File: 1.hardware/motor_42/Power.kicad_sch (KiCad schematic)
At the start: 24 parts, among them U1 TPS54202DDC

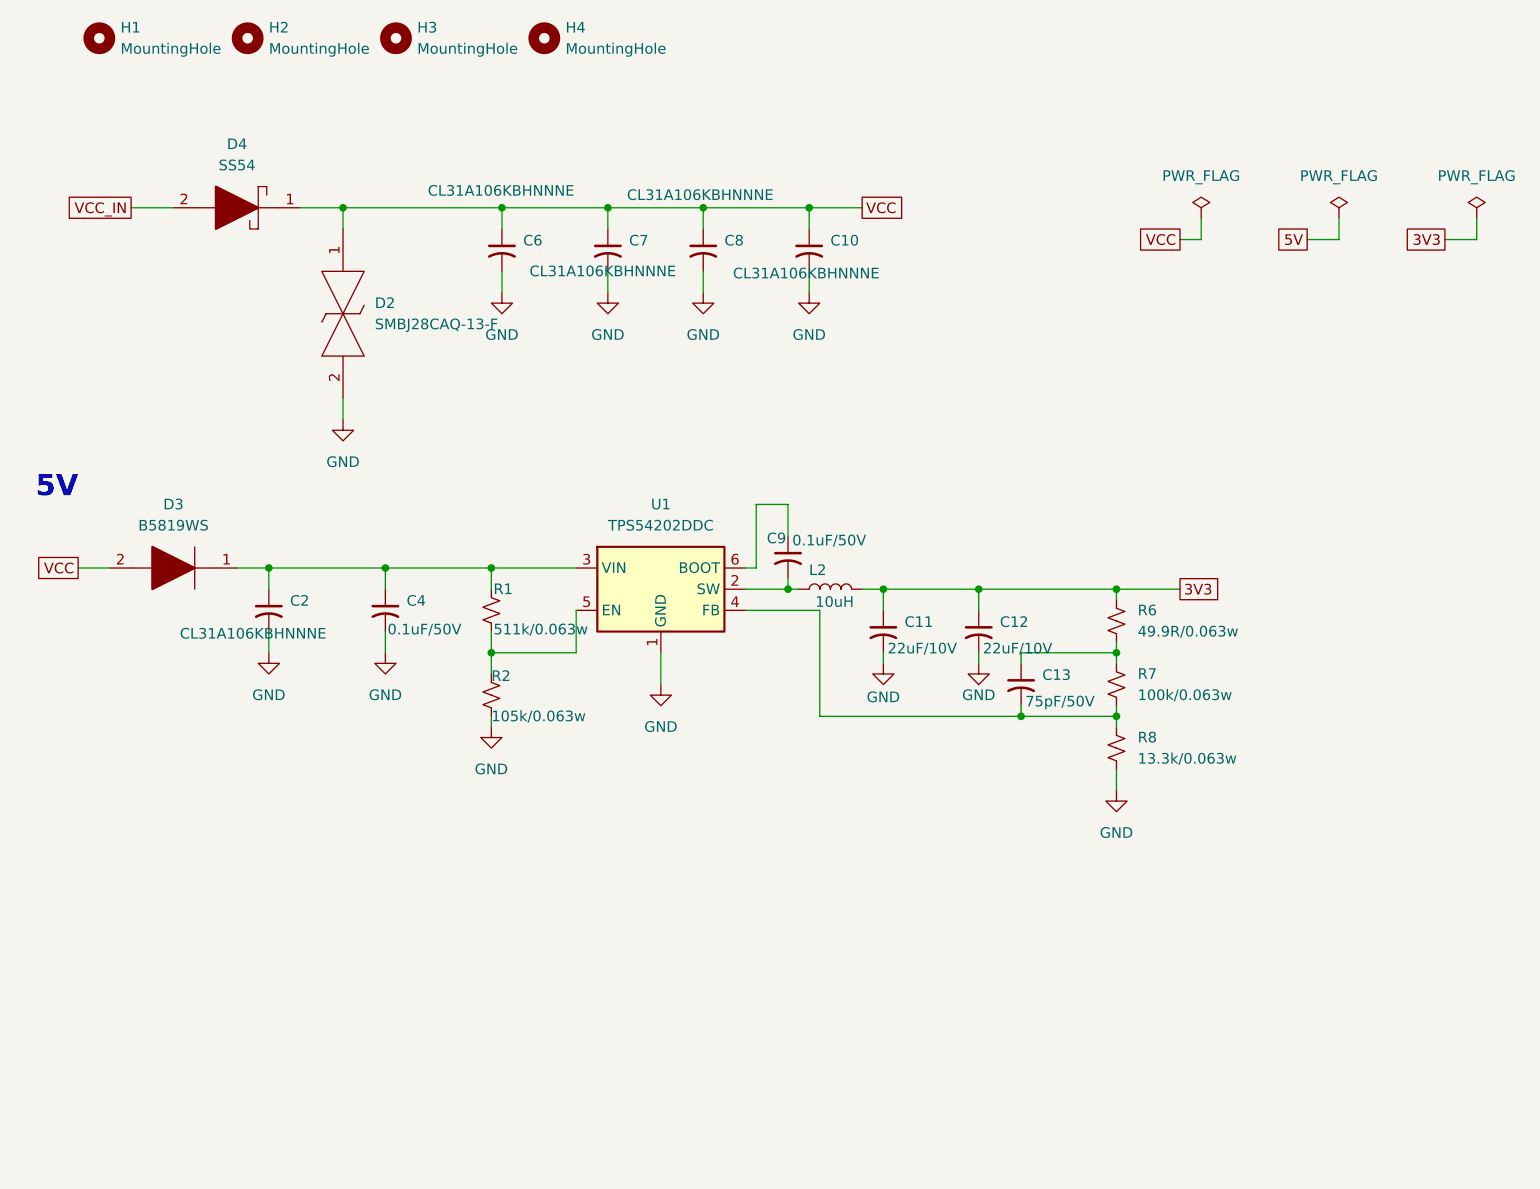
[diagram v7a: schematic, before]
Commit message: 번호 초기화 및 led 변경
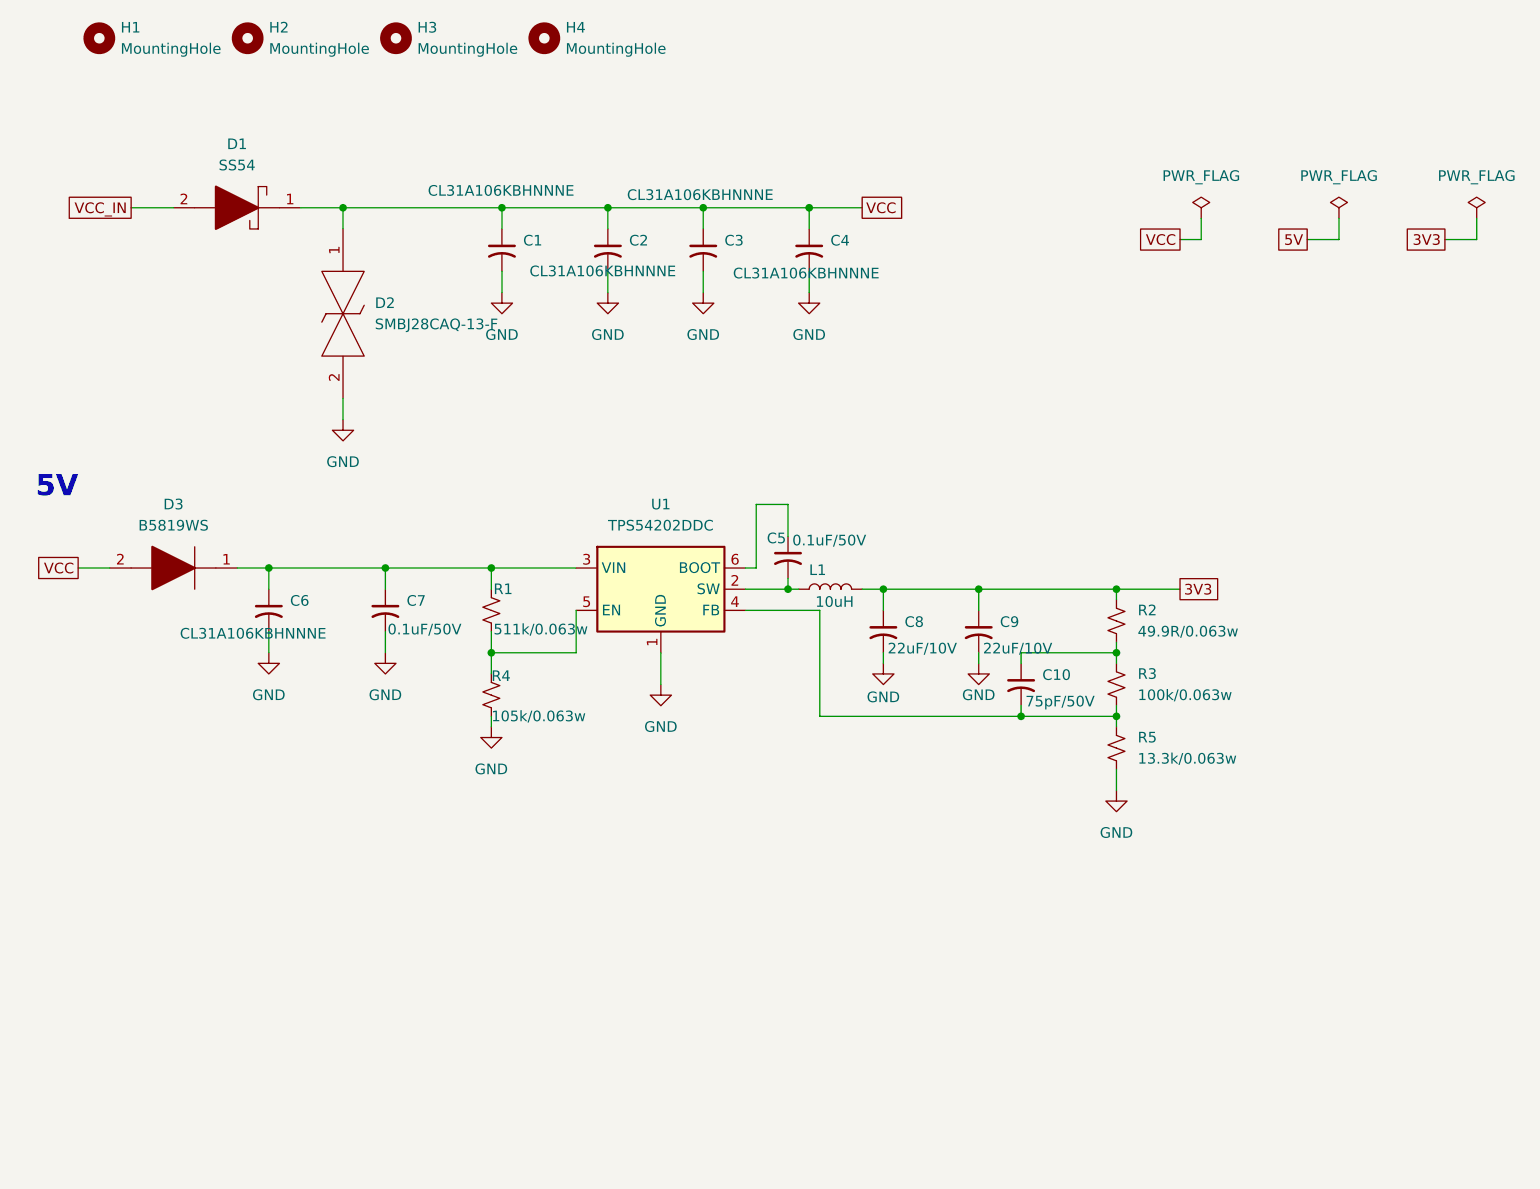
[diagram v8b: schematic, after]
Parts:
- renumbered C6 to C1, C13 to C10, C7 to C2, C8 to C3, C10 to C4, C9 to C5, C2 to C6, C4 to C7, C11 to C8, C12 to C9, D4 to D1, L2 to L1, R6 to R2, R7 to R3, R2 to R4, R8 to R5
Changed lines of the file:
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@@
 		(on_board yes)
 		(dnp no)
-		(property "Reference" "C2"
+		(property "Reference" "C6"
 			(at 57.15 92.8369 0)
 			(effects
@@
 			(project ""
 				(path "/3c5de6a8-6840-43a5-a2fb-24dbb7f0450d/79279b58-6f84-47a5-8a20-31a3cd7584cf"
-					(reference "C2")
+					(reference "C6")
 					(unit 1)
 				)
@@
 		(dnp no)
 		(fields_autoplaced yes)
-		(property "Reference" "#PWR02"
+		(property "Reference" "#PWR06"
 			(at 54.61 105.41 0)
 			(effects
@@
 			(project "motor_42"
 				(path "/3c5de6a8-6840-43a5-a2fb-24dbb7f0450d/79279b58-6f84-47a5-8a20-31a3cd7584cf"
-					(reference "#PWR02")
+					(reference "#PWR06")
 					(unit 1)
 				)
@@
 		(dnp no)
 		(fields_autoplaced yes)
-		(property "Reference" "D4"
+		(property "Reference" "D1"
 			(at 50.8 38.1 0)
 			(effects
@@
 			(project ""
 				(path "/3c5de6a8-6840-43a5-a2fb-24dbb7f0450d/79279b58-6f84-47a5-8a20-31a3cd7584cf"
-					(reference "D4")
+					(reference "D1")
 					(unit 1)
 				)
@@
 		(on_board yes)
 		(dnp no)
-		(property "Reference" "C6"
+		(property "Reference" "C1"
 			(at 85.09 49.6569 0)
 			(effects
@@
 			(project "motor_42"
 				(path "/3c5de6a8-6840-43a5-a2fb-24dbb7f0450d/79279b58-6f84-47a5-8a20-31a3cd7584cf"
-					(reference "C6")
+					(reference "C1")
 					(unit 1)
 				)
@@
 		(on_board yes)
 		(dnp no)
-		(property "Reference" "L2"
+		(property "Reference" "L1"
 			(at 120.396 89.154 90)
 			(effects
@@
 			(project ""
 				(path "/3c5de6a8-6840-43a5-a2fb-24dbb7f0450d/79279b58-6f84-47a5-8a20-31a3cd7584cf"
-					(reference "L2")
+					(reference "L1")
 					(unit 1)
 				)
@@
 		(dnp no)
 		(fields_autoplaced yes)
-		(property "Reference" "#PWR016"
+		(property "Reference" "#PWR012"
 			(at 156.21 121.92 0)
 			(effects
@@
 			(project "motor_42"
 				(path "/3c5de6a8-6840-43a5-a2fb-24dbb7f0450d/79279b58-6f84-47a5-8a20-31a3cd7584cf"
-					(reference "#PWR016")
+					(reference "#PWR012")
 					(unit 1)
 				)
@@
 		(on_board yes)
 		(dnp no)
-		(property "Reference" "C10"
+		(property "Reference" "C4"
 			(at 121.92 49.6569 0)
 			(effects
@@
 			(project "motor_42"
 				(path "/3c5de6a8-6840-43a5-a2fb-24dbb7f0450d/79279b58-6f84-47a5-8a20-31a3cd7584cf"
-					(reference "C10")
+					(reference "C4")
 					(unit 1)
 				)
@@
 		(dnp no)
 		(fields_autoplaced yes)
-		(property "Reference" "#PWR011"
+		(property "Reference" "#PWR03"
 			(at 106.68 62.23 0)
 			(effects
@@
 			(project "motor_42"
 				(path "/3c5de6a8-6840-43a5-a2fb-24dbb7f0450d/79279b58-6f84-47a5-8a20-31a3cd7584cf"
-					(reference "#PWR011")
+					(reference "#PWR03")
 					(unit 1)
 				)
@@
 		(on_board yes)
 		(dnp no)
-		(property "Reference" "R2"
+		(property "Reference" "R4"
 			(at 81.28 101.854 0)
 			(effects
@@
 			(project "motor_42"
 				(path "/3c5de6a8-6840-43a5-a2fb-24dbb7f0450d/79279b58-6f84-47a5-8a20-31a3cd7584cf"
-					(reference "R2")
+					(reference "R4")
 					(unit 1)
 				)
@@
 		(on_board yes)
 		(dnp no)
-		(property "Reference" "C13"
+		(property "Reference" "C10"
 			(at 147.32 101.7269 0)
 			(effects
@@
 			(project "motor_42"
 				(path "/3c5de6a8-6840-43a5-a2fb-24dbb7f0450d/79279b58-6f84-47a5-8a20-31a3cd7584cf"
-					(reference "C13")
+					(reference "C10")
 					(unit 1)
 				)
@@
 		(dnp no)
 		(fields_autoplaced yes)
-		(property "Reference" "R6"
+		(property "Reference" "R2"
 			(at 158.75 93.9799 0)
 			(effects
@@
 			(project "motor_42"
 				(path "/3c5de6a8-6840-43a5-a2fb-24dbb7f0450d/79279b58-6f84-47a5-8a20-31a3cd7584cf"
-					(reference "R6")
+					(reference "R2")
 					(unit 1)
 				)
@@
 		(on_board yes)
 		(dnp no)
-		(property "Reference" "C4"
+		(property "Reference" "C7"
 			(at 71.12 92.8369 0)
 			(effects
@@
 			(project "motor_42"
 				(path "/3c5de6a8-6840-43a5-a2fb-24dbb7f0450d/79279b58-6f84-47a5-8a20-31a3cd7584cf"
-					(reference "C4")
+					(reference "C7")
 					(unit 1)
 				)
@@
 		(dnp no)
 		(fields_autoplaced yes)
-		(property "Reference" "#PWR013"
+		(property "Reference" "#PWR04"
 			(at 119.38 62.23 0)
 			(effects
@@
 			(project "motor_42"
 				(path "/3c5de6a8-6840-43a5-a2fb-24dbb7f0450d/79279b58-6f84-47a5-8a20-31a3cd7584cf"
-					(reference "#PWR013")
+					(reference "#PWR04")
 					(unit 1)
 				)
@@
 		(dnp no)
 		(fields_autoplaced yes)
-		(property "Reference" "#PWR04"
+		(property "Reference" "#PWR05"
 			(at 63.5 77.47 0)
 			(effects
@@
 			(project "motor_42"
 				(path "/3c5de6a8-6840-43a5-a2fb-24dbb7f0450d/79279b58-6f84-47a5-8a20-31a3cd7584cf"
-					(reference "#PWR04")
+					(reference "#PWR05")
 					(unit 1)
 				)
@@
 		(dnp no)
 		(fields_autoplaced yes)
-		(property "Reference" "R8"
+		(property "Reference" "R5"
 			(at 158.75 109.2199 0)
 			(effects
@@
 			(project "motor_42"
 				(path "/3c5de6a8-6840-43a5-a2fb-24dbb7f0450d/79279b58-6f84-47a5-8a20-31a3cd7584cf"
-					(reference "R8")
+					(reference "R5")
 					(unit 1)
 				)
@@
 		(on_board yes)
 		(dnp no)
-		(property "Reference" "C7"
+		(property "Reference" "C2"
 			(at 97.79 49.6569 0)
 			(effects
@@
 			(project "motor_42"
 				(path "/3c5de6a8-6840-43a5-a2fb-24dbb7f0450d/79279b58-6f84-47a5-8a20-31a3cd7584cf"
-					(reference "C7")
+					(reference "C2")
 					(unit 1)
 				)
@@
 		(on_board yes)
 		(dnp no)
-		(property "Reference" "#PWR015"
+		(property "Reference" "#PWR09"
 			(at 139.7 106.68 0)
 			(effects
@@
 			(project "motor_42"
 				(path "/3c5de6a8-6840-43a5-a2fb-24dbb7f0450d/79279b58-6f84-47a5-8a20-31a3cd7584cf"
-					(reference "#PWR015")
+					(reference "#PWR09")
 					(unit 1)
 				)
@@
 		(dnp no)
 		(fields_autoplaced yes)
-		(property "Reference" "#PWR09"
+		(property "Reference" "#PWR02"
 			(at 95.25 62.23 0)
 			(effects
@@
 			(project "motor_42"
 				(path "/3c5de6a8-6840-43a5-a2fb-24dbb7f0450d/79279b58-6f84-47a5-8a20-31a3cd7584cf"
-					(reference "#PWR09")
+					(reference "#PWR02")
 					(unit 1)
 				)
@@
 		(dnp no)
 		(fields_autoplaced yes)
-		(property "Reference" "R7"
+		(property "Reference" "R3"
 			(at 158.75 101.5999 0)
 			(effects
@@
 			(project ""
 				(path "/3c5de6a8-6840-43a5-a2fb-24dbb7f0450d/79279b58-6f84-47a5-8a20-31a3cd7584cf"
-					(reference "R7")
+					(reference "R3")
 					(unit 1)
 				)
@@
 		(dnp no)
 		(fields_autoplaced yes)
-		(property "Reference" "#PWR08"
+		(property "Reference" "#PWR01"
 			(at 82.55 62.23 0)
 			(effects
@@
 			(project "motor_42"
 				(path "/3c5de6a8-6840-43a5-a2fb-24dbb7f0450d/79279b58-6f84-47a5-8a20-31a3cd7584cf"
-					(reference "#PWR08")
+					(reference "#PWR01")
 					(unit 1)
 				)
@@
 		(on_board yes)
 		(dnp no)
-		(property "Reference" "#PWR014"
+		(property "Reference" "#PWR08"
 			(at 128.27 106.68 0)
 			(effects
@@
 			(project "motor_42"
 				(path "/3c5de6a8-6840-43a5-a2fb-24dbb7f0450d/79279b58-6f84-47a5-8a20-31a3cd7584cf"
-					(reference "#PWR014")
+					(reference "#PWR08")
 					(unit 1)
 				)
@@
 		(on_board yes)
 		(dnp no)
-		(property "Reference" "C11"
+		(property "Reference" "C8"
 			(at 130.81 95.3769 0)
 			(effects
@@
 			(project "motor_42"
 				(path "/3c5de6a8-6840-43a5-a2fb-24dbb7f0450d/79279b58-6f84-47a5-8a20-31a3cd7584cf"
-					(reference "C11")
+					(reference "C8")
 					(unit 1)
 				)
@@
 		(dnp no)
 		(fields_autoplaced yes)
-		(property "Reference" "#PWR07"
+		(property "Reference" "#PWR011"
 			(at 81.28 114.3 0)
 			(effects
@@
 			(project "motor_42"
 				(path "/3c5de6a8-6840-43a5-a2fb-24dbb7f0450d/79279b58-6f84-47a5-8a20-31a3cd7584cf"
-					(reference "#PWR07")
+					(reference "#PWR011")
 					(unit 1)
 				)
@@
 		(dnp no)
 		(fields_autoplaced yes)
-		(property "Reference" "#PWR05"
+		(property "Reference" "#PWR07"
 			(at 68.58 105.41 0)
 			(effects
@@
 			(project "motor_42"
 				(path "/3c5de6a8-6840-43a5-a2fb-24dbb7f0450d/79279b58-6f84-47a5-8a20-31a3cd7584cf"
-					(reference "#PWR05")
+					(reference "#PWR07")
 					(unit 1)
 				)
@@
 		(on_board yes)
 		(dnp no)
-		(property "Reference" "C8"
+		(property "Reference" "C3"
 			(at 109.22 49.6569 0)
 			(effects
@@
 			(project "motor_42"
 				(path "/3c5de6a8-6840-43a5-a2fb-24dbb7f0450d/79279b58-6f84-47a5-8a20-31a3cd7584cf"
-					(reference "C8")
+					(reference "C3")
 					(unit 1)
 				)
@@
 		(on_board yes)
 		(dnp no)
-		(property "Reference" "C9"
+		(property "Reference" "C5"
 			(at 114.3 85.344 0)
 			(effects
@@
 			(project "motor_42"
 				(path "/3c5de6a8-6840-43a5-a2fb-24dbb7f0450d/79279b58-6f84-47a5-8a20-31a3cd7584cf"
-					(reference "C9")
+					(reference "C5")
 					(unit 1)
 				)
@@
 		(on_board yes)
 		(dnp no)
-		(property "Reference" "C12"
+		(property "Reference" "C9"
 			(at 142.24 95.3769 0)
 			(effects
@@
 			(project "motor_42"
 				(path "/3c5de6a8-6840-43a5-a2fb-24dbb7f0450d/79279b58-6f84-47a5-8a20-31a3cd7584cf"
-					(reference "C12")
-					(unit 1)
-				)
+					(reference "C9")
+					(unit 1)
+				)
